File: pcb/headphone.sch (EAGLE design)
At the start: 29 parts, among them IC101 LF353D, IC201 LF353N, IC301 LF353N, J101 MONOJACKSWITCHCRAFT3, J102 MONOJACKSWITCHCRAFT3, J201 MONOJACKNEUTRIK, J202 MONOJACKNEUTRIK, J301 STEREOJACK, J401 POWER_SIMPLE16, P101 DUALPOT 50K

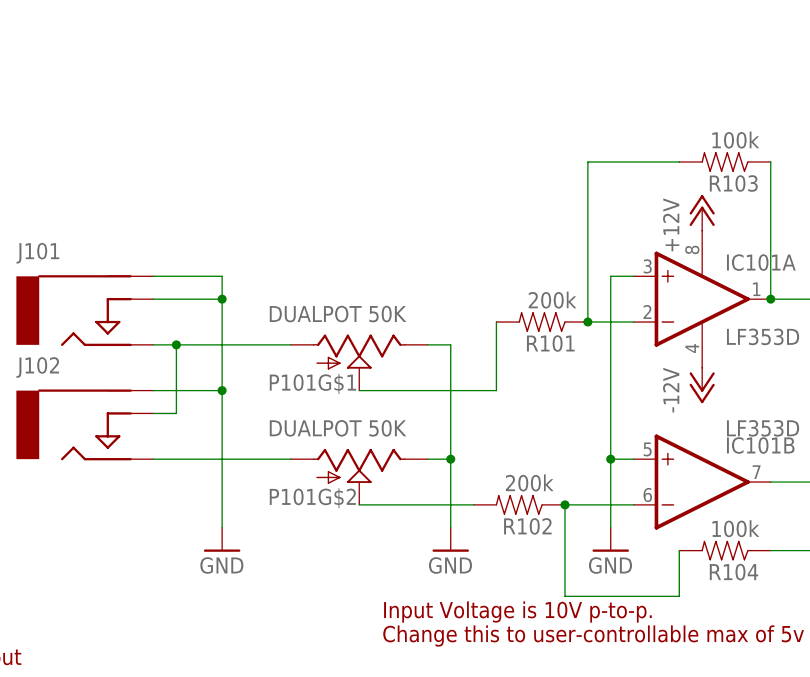
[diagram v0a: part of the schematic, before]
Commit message: fix for backwards volume knob and too-small text
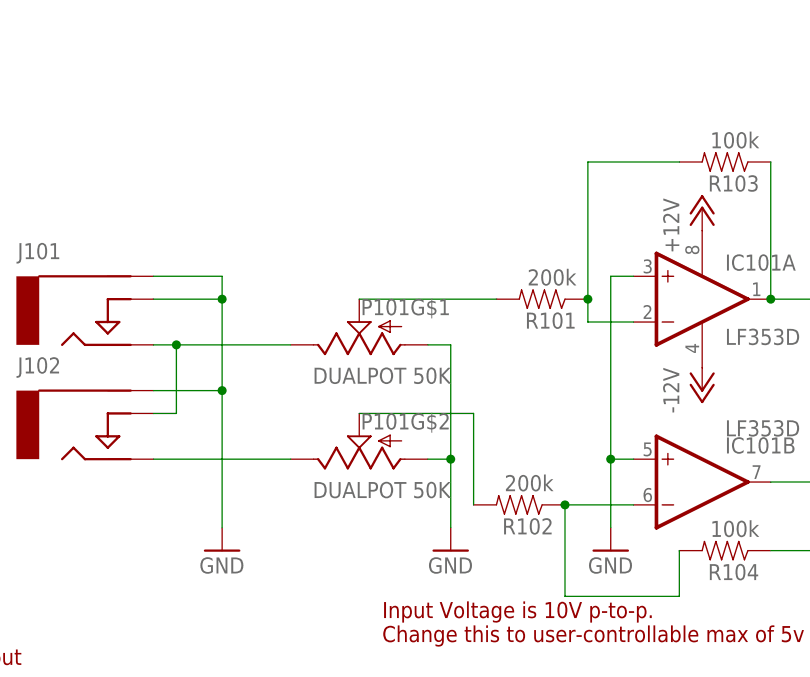
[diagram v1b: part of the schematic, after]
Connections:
- removed net N$3 (its old number): J102.TIP, P101G$2.A
- new net N$5: J102.TIP, P101G$2.E
- net GND: now also P101G$1.A, P101G$2.A; no longer P101G$1.E, P101G$2.E
- net J102: now also P101G$1.E; no longer P101G$1.A
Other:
- moved on the sheet: P101G$1, P101G$2, R101
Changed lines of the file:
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@@
 <attribute name="VALUE" x="88.9" y="134.62" size="1.778" layer="96"/>
 </instance>
-<instance part="P101" gate="G$1" x="48.26" y="144.78" rot="R270"/>
-<instance part="P101" gate="G$2" x="48.26" y="132.08" rot="R270"/>
+<instance part="P101" gate="G$1" x="48.26" y="144.78" rot="R90"/>
+<instance part="P101" gate="G$2" x="48.26" y="132.08" rot="R90"/>
 <instance part="GND3" gate="1" x="58.42" y="121.92"/>
 <instance part="IC101" gate="P" x="86.36" y="149.86"/>
@@
 <instance part="P-2" gate="1" x="86.36" y="139.7"/>
 <instance part="R102" gate="G$1" x="66.04" y="127" rot="R180"/>
-<instance part="R101" gate="G$1" x="68.58" y="147.32" rot="R180"/>
+<instance part="R101" gate="G$1" x="68.58" y="149.86" rot="R180"/>
 <instance part="GND4" gate="1" x="76.2" y="121.92"/>
 <instance part="R104" gate="G$1" x="88.9" y="121.92" rot="R180"/>
@@
 </segment>
 <segment>
-<pinref part="P101" gate="G$1" pin="E"/>
+<wire x1="58.42" y1="144.78" x2="58.42" y2="132.08" width="0.1524" layer="91"/>
+<pinref part="GND3" gate="1" pin="GND"/>
+<pinref part="P101" gate="G$1" pin="A"/>
+<wire x1="58.42" y1="132.08" x2="58.42" y2="124.46" width="0.1524" layer="91"/>
 <wire x1="55.88" y1="144.78" x2="58.42" y2="144.78" width="0.1524" layer="91"/>
-<wire x1="58.42" y1="144.78" x2="58.42" y2="132.08" width="0.1524" layer="91"/>
-<pinref part="P101" gate="G$2" pin="E"/>
-<wire x1="58.42" y1="132.08" x2="58.42" y2="124.46" width="0.1524" layer="91"/>
+<pinref part="P101" gate="G$2" pin="A"/>
 <wire x1="55.88" y1="132.08" x2="58.42" y2="132.08" width="0.1524" layer="91"/>
 <junction x="58.42" y="132.08"/>
-<pinref part="GND3" gate="1" pin="GND"/>
 </segment>
 <segment>
@@
 <wire x1="27.94" y1="144.78" x2="27.94" y2="137.16" width="0.1524" layer="91"/>
 <wire x1="27.94" y1="137.16" x2="25.4" y2="137.16" width="0.1524" layer="91"/>
-<wire x1="27.94" y1="144.78" x2="40.64" y2="144.78" width="0.1524" layer="91"/>
-<junction x="27.94" y="144.78"/>
-<pinref part="P101" gate="G$1" pin="A"/>
 <pinref part="J101" gate="J$1" pin="TIP"/>
 <pinref part="J102" gate="J$1" pin="NORM"/>
-</segment>
-</net>
-<net name="N$3" class="0">
-<segment>
-<wire x1="25.4" y1="132.08" x2="40.64" y2="132.08" width="0.1524" layer="91"/>
-<pinref part="P101" gate="G$2" pin="A"/>
-<pinref part="J102" gate="J$1" pin="TIP"/>
+<pinref part="P101" gate="G$1" pin="E"/>
+<wire x1="40.64" y1="144.78" x2="27.94" y2="144.78" width="0.1524" layer="91"/>
+<junction x="27.94" y="144.78"/>
 </segment>
 </net>
@@
 <net name="N$4" class="0">
 <segment>
-<pinref part="IC101" gate="A" pin="-IN"/>
 <pinref part="R101" gate="G$1" pin="1"/>
-<wire x1="78.74" y1="147.32" x2="73.66" y2="147.32" width="0.1524" layer="91"/>
 <pinref part="R103" gate="G$1" pin="2"/>
 <wire x1="83.82" y1="165.1" x2="73.66" y2="165.1" width="0.1524" layer="91"/>
-<wire x1="73.66" y1="165.1" x2="73.66" y2="147.32" width="0.1524" layer="91"/>
-<junction x="73.66" y="147.32"/>
-</segment>
-</net>
-<net name="N$5" class="0">
-<segment>
-<pinref part="R101" gate="G$1" pin="2"/>
-<wire x1="63.5" y1="147.32" x2="63.5" y2="139.7" width="0.1524" layer="91"/>
-<pinref part="P101" gate="G$1" pin="S"/>
-<wire x1="63.5" y1="139.7" x2="48.26" y2="139.7" width="0.1524" layer="91"/>
-</segment>
-</net>
-<net name="N$6" class="0">
-<segment>
-<pinref part="P101" gate="G$2" pin="S"/>
-<pinref part="R102" gate="G$1" pin="2"/>
-<wire x1="48.26" y1="127" x2="60.96" y2="127" width="0.1524" layer="91"/>
+<wire x1="73.66" y1="165.1" x2="73.66" y2="149.86" width="0.1524" layer="91"/>
+<wire x1="73.66" y1="149.86" x2="73.66" y2="147.32" width="0.1524" layer="91"/>
+<junction x="73.66" y="149.86"/>
+<pinref part="IC101" gate="A" pin="-IN"/>
+<wire x1="73.66" y1="147.32" x2="78.74" y2="147.32" width="0.1524" layer="91"/>
 </segment>
 </net>
@@
 </segment>
 </net>
+<net name="N$2" class="0">
+<segment>
+<pinref part="P101" gate="G$2" pin="S"/>
+<wire x1="48.26" y1="137.16" x2="60.96" y2="137.16" width="0.1524" layer="91"/>
+<pinref part="R102" gate="G$1" pin="2"/>
+<wire x1="60.96" y1="137.16" x2="60.96" y2="127" width="0.1524" layer="91"/>
+</segment>
+</net>
+<net name="N$3" class="0">
+<segment>
+<pinref part="P101" gate="G$1" pin="S"/>
+<wire x1="48.26" y1="149.86" x2="63.5" y2="149.86" width="0.1524" layer="91"/>
+<pinref part="R101" gate="G$1" pin="2"/>
+</segment>
+</net>
+<net name="N$5" class="0">
+<segment>
+<pinref part="J102" gate="J$1" pin="TIP"/>
+<pinref part="P101" gate="G$2" pin="E"/>
+<wire x1="25.4" y1="132.08" x2="40.64" y2="132.08" width="0.1524" layer="91"/>
+</segment>
+</net>
